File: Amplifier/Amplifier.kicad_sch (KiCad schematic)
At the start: 26 parts, among them U1 SKY65111-348LF, U2 MAX2633EUT+T

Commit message: updated schematic. resized sheet.
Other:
- note added: "DONT NEED PHASE SHIFTER BC THAT IS HANDLED BY LILYGO TRANSCEIVER CIRCUIT"
- note added: "Diode to ground?"
- note added: "LNA"
- note added: "Limiter"
- note added: "NOTES: 1. 2. 3. 4."
- note added: "Use potentiometers maybe fixed R stage 3 adjust stage1/2? >read datasheet"
- note added: "preamp???"
- note added: "switch w/ SPDT tie to optocoupler? 50ohm R to transmit line?"
- note removed: "Receive"
- note removed: "Use potentiometers maybe set stage 3 adjust stage1/2? >read datasheet"
- moved on the sheet: C1, C10, C11, C12, C13, C14, C15, C16, C17, C18, C19, C2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

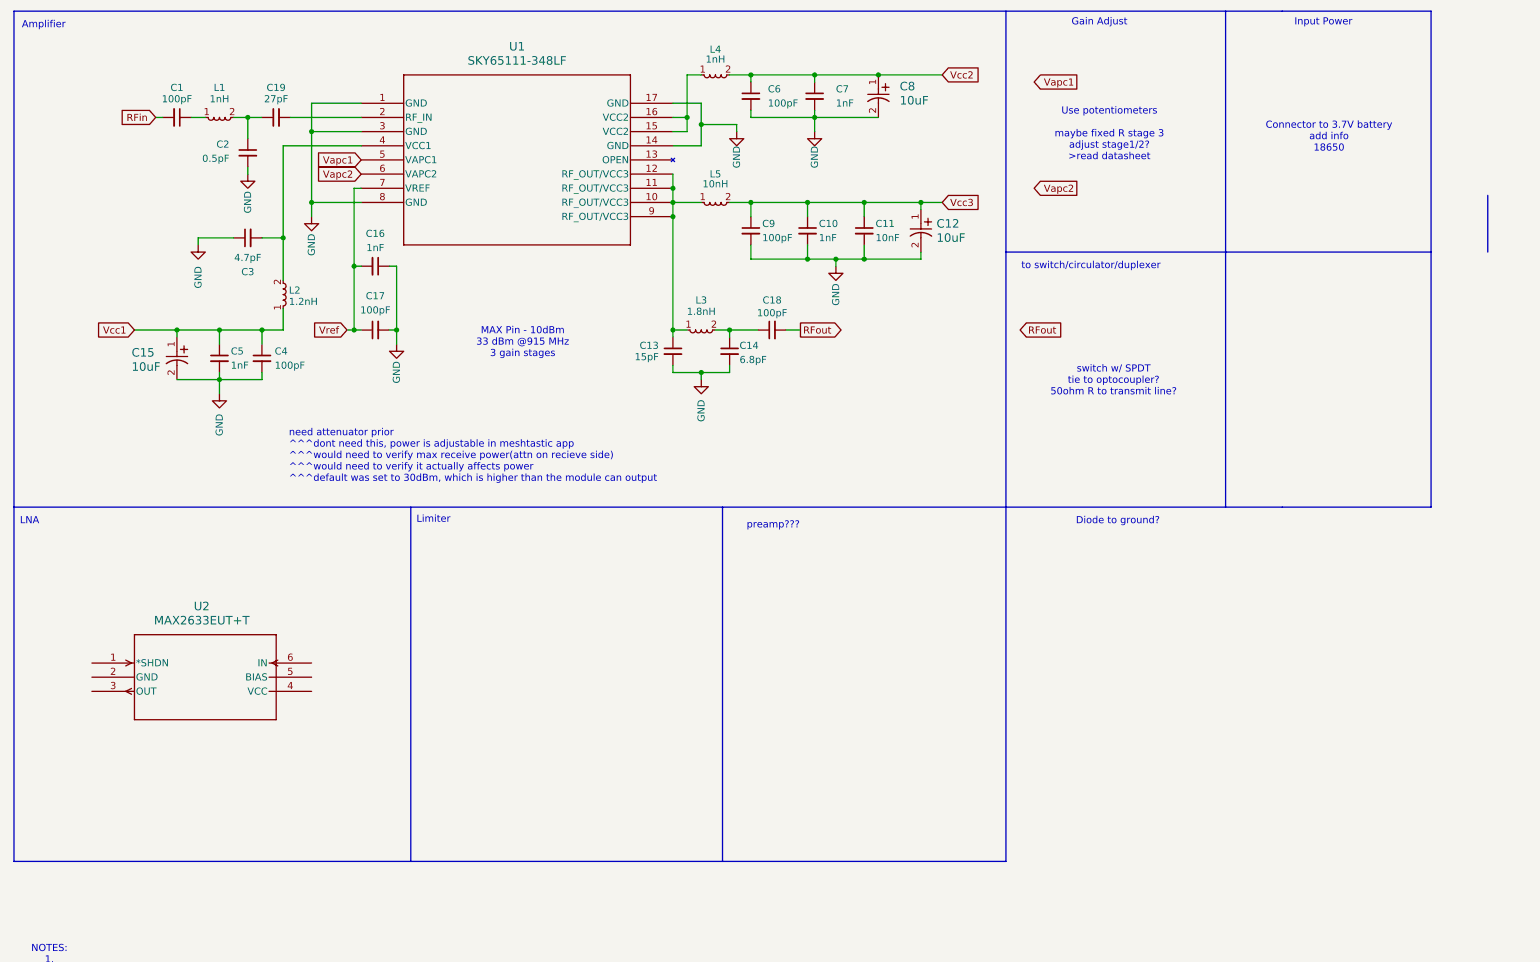
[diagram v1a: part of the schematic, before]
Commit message: added limiter to schematic/libraries. added notes to schematic.
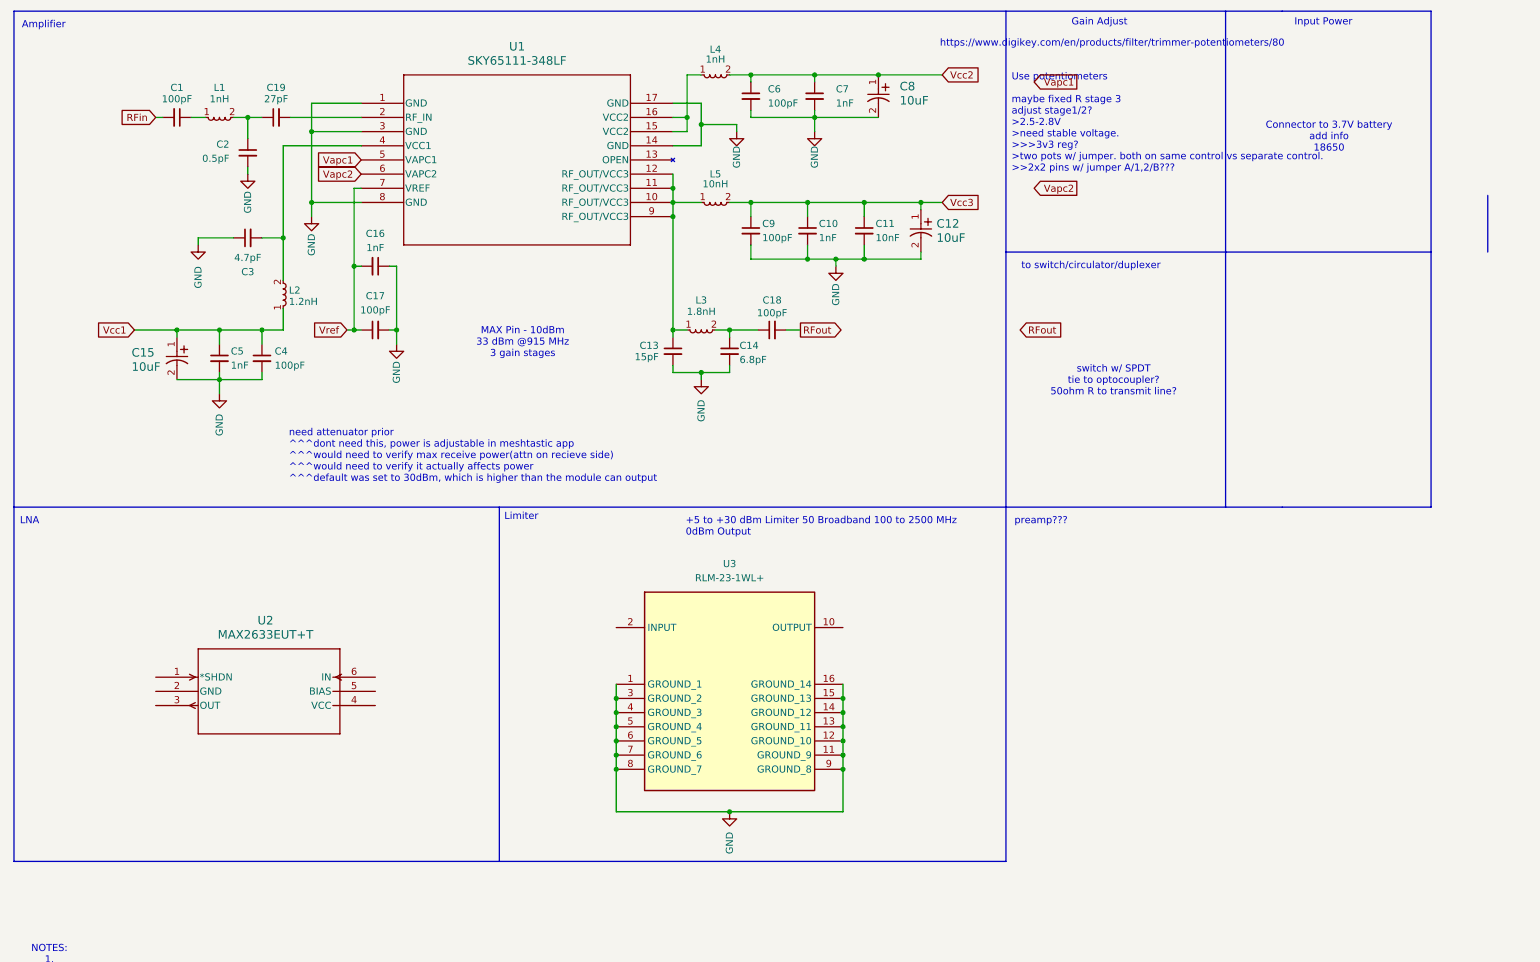
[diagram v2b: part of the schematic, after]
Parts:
- added U3: RLM-23-1WL+, amp:RLM231WL, symbol amp:RLM-23-1WL+
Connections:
- net GND: now also U3.1 (GROUND_1), U3.11 (GROUND_9), U3.12 (GROUND_10), U3.13 (GROUND_11), U3.14 (GROUND_12), U3.15 (GROUND_13), U3.16 (GROUND_14), U3.3 (GROUND_2), U3.4 (GROUND_3), U3.5 (GROUND_4), U3.6 (GROUND_5), U3.7 (GROUND_6), U3.8 (GROUND_7), U3.9 (GROUND_8)
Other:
- note added: "+5 to +30 dBm Limiter 50 Broadband 100 to 2500 MHz 0dBm Output"
- note added: "Use potentiometers maybe fixed R stage 3 adjust stage1/2? >2.5-2.8V >need stable voltage. >>>3v3 reg? >two pots w/ jumper. both on same control vs separate control. >>2x2 pins w/ jumper A/1,2/B???"
- note added: "https://www.digikey.com/en/products/filter/trimmer-potentiometers/80"
- note removed: "Diode to ground?"
- note removed: "Use potentiometers maybe fixed R stage 3 adjust stage1/2? >read datasheet"
- moved on the sheet: U2

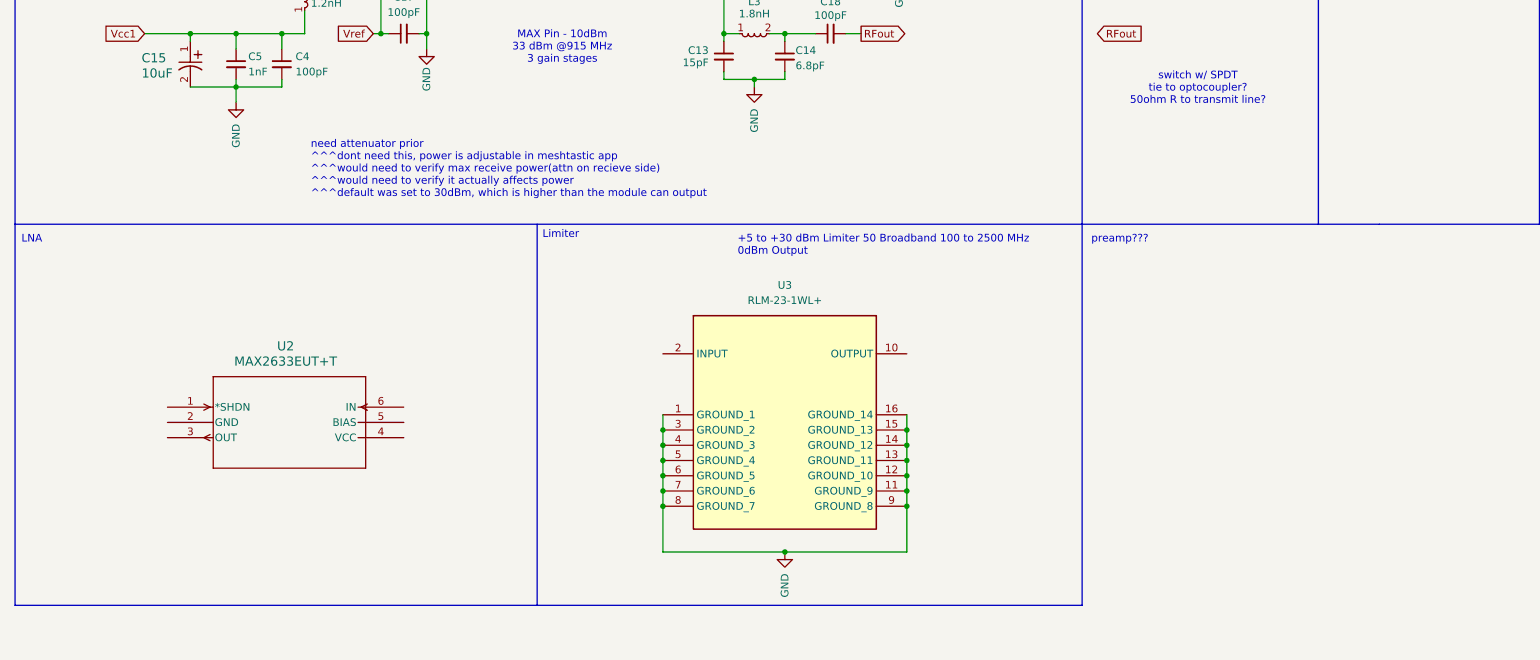
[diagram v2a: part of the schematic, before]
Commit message: updated schematic notes.
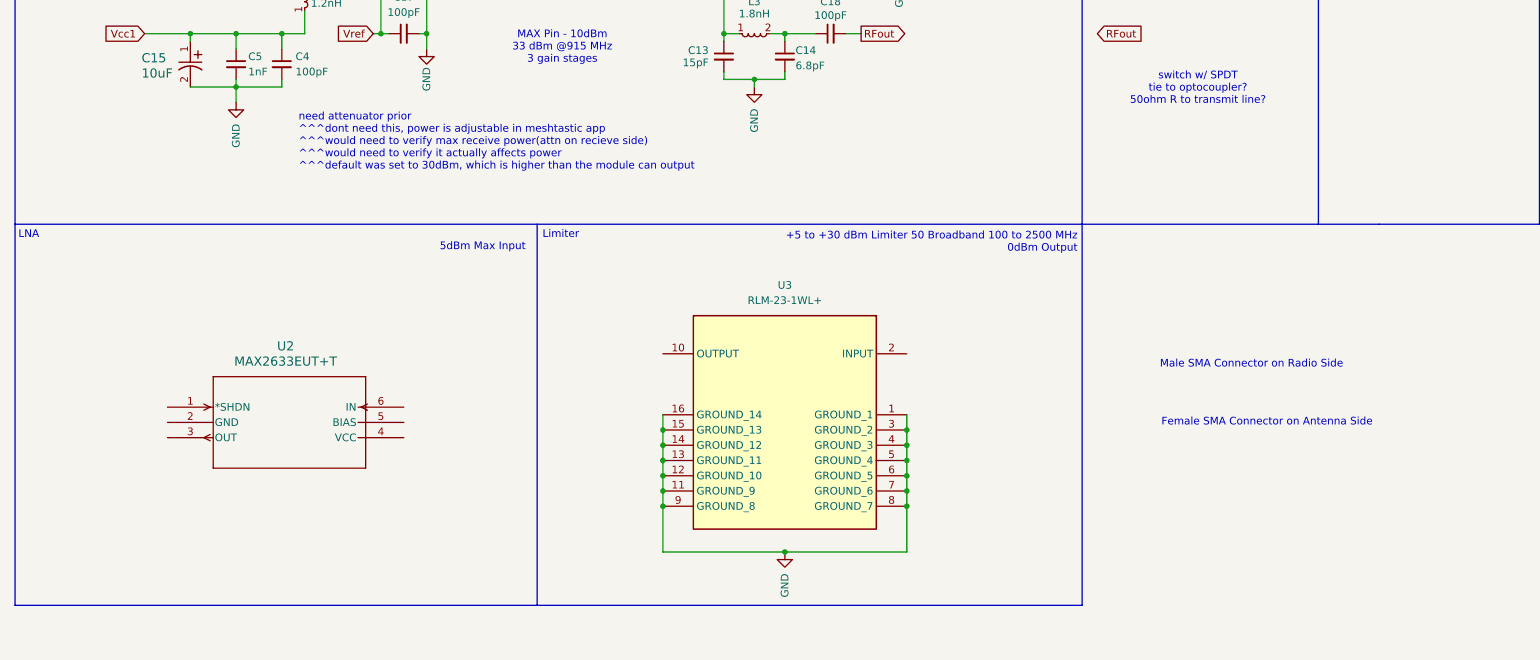
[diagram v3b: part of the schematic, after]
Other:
- note added: "5dBm Max Input"
- note added: "Female SMA Connector on Antenna Side"
- note added: "Male SMA Connector on Radio Side"
- note removed: "preamp???"
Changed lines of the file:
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@@
 	(title_block
 		(title "915Mhz Amp")
-		(date "2026-08-22")
+		(date "2026-09-01")
 		(rev "0")
 	)
@@
 		)
 	)
-	(text "preamp???"
+	(text "Male SMA Connector on Radio Side"
 		(exclude_from_sim no)
-		(at 192.024 104.14 0)
+		(at 203.454 124.968 0)
 		(effects
 			(font
@@
 	(text "\nneed attenuator prior\n^^^dont need this, power is adjustable in meshtastic app\n^^^would need to verify max receive power(attn on recieve side) \n^^^would need to verify it actually affects power\n^^^default was set to 30dBm, which is higher than the module can output\n"
 		(exclude_from_sim no)
-		(at 61.976 91.44 0)
+		(at 59.944 86.868 0)
 		(effects
 			(font
@@
 		)
 	)
+	(text "5dBm Max Input"
+		(exclude_from_sim no)
+		(at 97.79 105.41 0)
+		(effects
+			(font
+				(size 1.27 1.27)
+			)
+			(justify right)
+		)
+	)
 	(text "Gain Adjust"
 		(exclude_from_sim no)
@@
 	(text "+5 to +30 dBm Limiter 50 Broadband 100 to 2500 MHz\n0dBm Output"
 		(exclude_from_sim no)
-		(at 133.096 105.156 0)
+		(at 189.738 104.648 0)
 		(effects
 			(font
 				(size 1.27 1.27)
 			)
-			(justify left)
+			(justify right)
 		)
 	)
@@
 	(text "LNA"
 		(exclude_from_sim no)
-		(at 15.494 104.14 0)
+		(at 14.986 103.378 0)
 		(effects
 			(font
@@
 		)
 	)
+	(text "Female SMA Connector on Antenna Side"
+		(exclude_from_sim no)
+		(at 203.708 134.62 0)
+		(effects
+			(font
+				(size 1.27 1.27)
+			)
+			(justify left)
+		)
+	)
 	(text "Limiter"
 		(exclude_from_sim no)
@@
 	)
 	(junction
-		(at 120.65 146.05)
-		(diameter 0)
-		(color 0 0 0 0)
-	)
-	(junction
 		(at 161.29 140.97)
 		(diameter 0)
@@
 	)
 	(junction
-		(at 161.29 143.51)
-		(diameter 0)
-		(color 0 0 0 0)
-	)
-	(junction
 		(at 130.81 46.99)
 		(diameter 0)
@@
 	)
 	(junction
-		(at 167.64 24.13)
+		(at 161.29 143.51)
 		(diameter 0)
 		(color 0 0 0 0)
 	)
 	(junction
-		(at 120.65 148.59)
+		(at 167.64 24.13)
 		(diameter 0)
 		(color 0 0 0 0)
@@
 	)
 	(junction
+		(at 120.65 148.59)
+		(diameter 0)
+		(color 0 0 0 0)
+	)
+	(junction
+		(at 161.29 148.59)
+		(diameter 0)
+		(color 0 0 0 0)
+	)
+	(junction
 		(at 120.65 140.97)
 		(diameter 0)
@@
 	)
 	(junction
-		(at 156.21 24.13)
+		(at 120.65 146.05)
 		(diameter 0)
 		(color 0 0 0 0)
 	)
 	(junction
-		(at 165.1 46.99)
+		(at 156.21 24.13)
 		(diameter 0)
 		(color 0 0 0 0)
 	)
 	(junction
-		(at 57.15 69.85)
+		(at 165.1 46.99)
 		(diameter 0)
 		(color 0 0 0 0)
 	)
 	(junction
-		(at 140.97 156.21)
+		(at 57.15 69.85)
 		(diameter 0)
 		(color 0 0 0 0)
 	)
 	(junction
-		(at 161.29 146.05)
+		(at 140.97 156.21)
 		(diameter 0)
 		(color 0 0 0 0)
@@
 	)
 	(junction
-		(at 161.29 148.59)
+		(at 66.04 46.99)
 		(diameter 0)
 		(color 0 0 0 0)
 	)
 	(junction
-		(at 66.04 46.99)
+		(at 120.65 143.51)
 		(diameter 0)
 		(color 0 0 0 0)
@@
 	)
 	(junction
-		(at 120.65 143.51)
+		(at 161.29 146.05)
 		(diameter 0)
 		(color 0 0 0 0)
@@
 	(wire
 		(pts
-			(xy 120.65 146.05) (xy 120.65 143.51)
-		)
-		(stroke
-			(width 0)
-			(type default)
-		)
-	)
-	(wire
-		(pts
 			(xy 130.81 69.85) (xy 133.35 69.85)
 		)
@@
 	(wire
 		(pts
-			(xy 81.28 58.42) (xy 81.28 69.85)
+			(xy 161.29 143.51) (xy 161.29 146.05)
 		)
 		(stroke
@@
 	(wire
 		(pts
-			(xy 161.29 143.51) (xy 161.29 146.05)
+			(xy 81.28 58.42) (xy 81.28 69.85)
 		)
 		(stroke
@@
 	(wire
 		(pts
-			(xy 133.35 31.75) (xy 133.35 34.29)
+			(xy 161.29 140.97) (xy 161.29 143.51)
 		)
 		(stroke
@@
 	(wire
 		(pts
-			(xy 161.29 135.89) (xy 161.29 138.43)
+			(xy 133.35 31.75) (xy 133.35 34.29)
 		)
 		(stroke
@@
 	(wire
 		(pts
-			(xy 120.65 148.59) (xy 120.65 146.05)
+			(xy 161.29 135.89) (xy 161.29 138.43)
 		)
 		(stroke
@@
 	(wire
 		(pts
-			(xy 120.65 156.21) (xy 120.65 148.59)
+			(xy 120.65 148.59) (xy 120.65 156.21)
+		)
+		(stroke
+			(width 0)
+			(type default)
+		)
+	)
+	(wire
+		(pts
+			(xy 161.29 146.05) (xy 161.29 148.59)
 		)
 		(stroke
@@
 	(wire
 		(pts
-			(xy 161.29 146.05) (xy 161.29 148.59)
+			(xy 66.04 34.29) (xy 74.93 34.29)
 		)
 		(stroke
@@
 	(wire
 		(pts
-			(xy 66.04 34.29) (xy 74.93 34.29)
+			(xy 165.1 46.99) (xy 175.26 46.99)
 		)
 		(stroke
@@
 	(wire
 		(pts
-			(xy 165.1 46.99) (xy 175.26 46.99)
+			(xy 120.65 146.05) (xy 120.65 148.59)
 		)
 		(stroke
@@
 	(wire
 		(pts
-			(xy 120.65 143.51) (xy 120.65 140.97)
+			(xy 120.65 140.97) (xy 120.65 143.51)
 		)
 		(stroke
@@
 	(wire
 		(pts
-			(xy 161.29 140.97) (xy 161.29 143.51)
-		)
-		(stroke
-			(width 0)
-			(type default)
-		)
-	)
-	(wire
-		(pts
 			(xy 140.97 69.85) (xy 146.05 69.85)
 		)
@@
 		)
 	)
+	(wire
+		(pts
+			(xy 120.65 143.51) (xy 120.65 146.05)
+		)
+		(stroke
+			(width 0)
+			(type default)
+		)
+	)
 	(image
 		(at 379.73 113.03)
@@
 		(lib_id "amp:RLM-23-1WL+")
 		(at 140.97 137.16 0)
+		(mirror y)
 		(unit 1)
 		(body_style 1)
@@
 		(in_pos_files yes)
 		(dnp no)
-		(fields_autoplaced yes)
 		(property "Reference" "U3"
 			(at 140.97 111.76 0)
@@
 		)
 		(property "Footprint" "amp:RLM231WL"
-			(at 177.8 216.84 0)
+			(at 104.14 216.84 0)
 			(hide yes)
 			(show_name no)
@@
 		)
 		(property "Datasheet" "https://www.minicircuits.com/WebStore/dashboard.html?model=RLM-23-1WL%2B"
-			(at 177.8 316.84 0)
+			(at 104.14 316.84 0)
 			(hide yes)
 			(show_name no)
@@
 		)
 		(property "Description" "+5 to +30 dBm Limiter 50 Broadband 100 to 2500 MHz"
-			(at 111.252 102.87 0)
+			(at 170.688 102.87 0)
 			(hide yes)
 			(show_name no)
@@
 		)
 		(property "MFN" "Mini-Circuits"
-			(at 177.8 616.84 0)
+			(at 104.14 616.84 0)
 			(hide yes)
 			(show_name no)
@@
 		)
 		(property "MFP" "RLM-23-1WL+"
-			(at 177.8 716.84 0)
+			(at 104.14 716.84 0)
 			(hide yes)
 			(show_name no)
@@
 		)
 		(property "OctopartURL" "https://octopart.com/part/mini-circuits/RLM-23-1WL+"
-			(at 110.744 105.918 0)
+			(at 171.196 105.918 0)
 			(hide yes)
 			(show_name no)
@@
 		)
 		(property "LCSCPart" "C7288002"
-			(at 114.554 105.918 0)
+			(at 167.386 105.918 0)
 			(hide yes)
 			(show_name no)
